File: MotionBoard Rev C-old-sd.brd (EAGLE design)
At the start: 99 x 53.3 mm, 110 parts, among them IC1 LPC1769FBD100 or LPC4078FBD10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, IC2 LD1117, IC4 LMV324, Q1 NTGS3441T1G, Q2 12MHz, Q3 25MHz, U1 ARDUINO-FIREPICK+RAMPS, U2 101-00660-68-6, X2 USB-MICRO-B

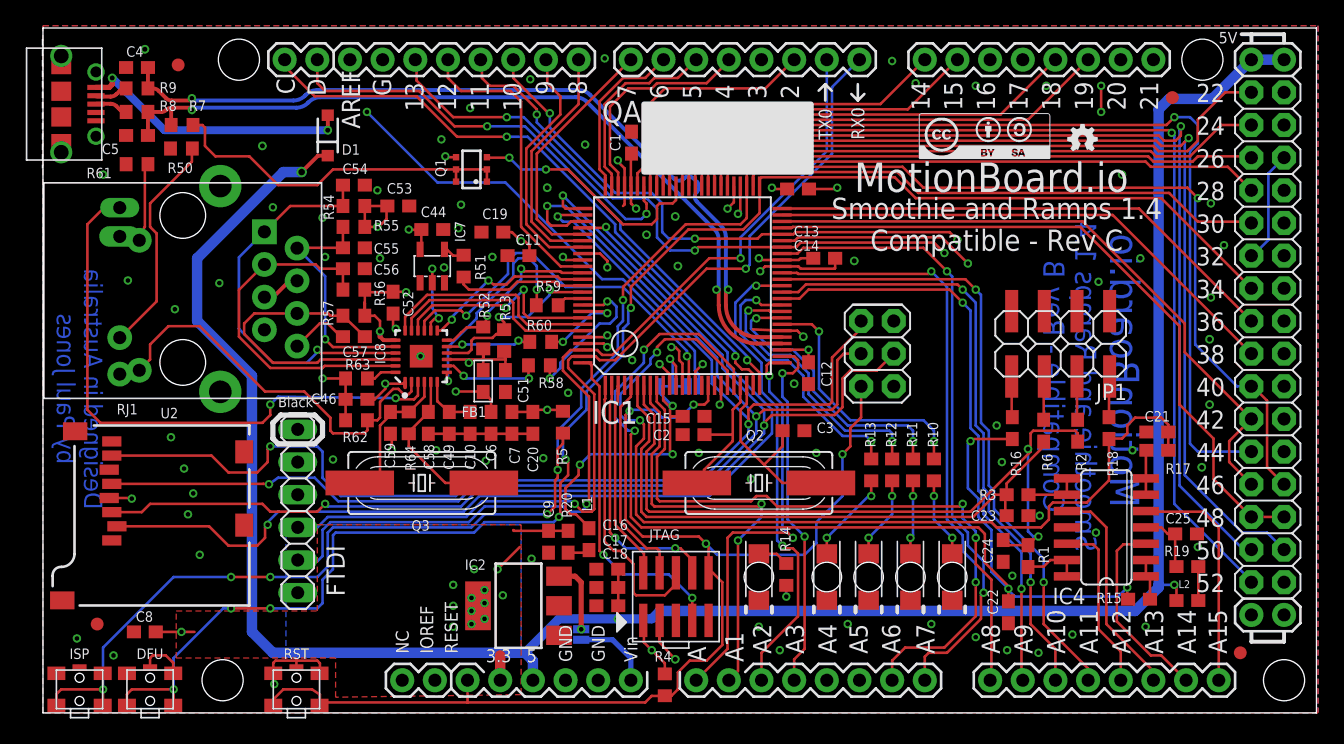
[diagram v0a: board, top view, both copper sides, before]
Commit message: Update component values
Signed-off-by: Paul Jones <paul@pauljones.id.au>
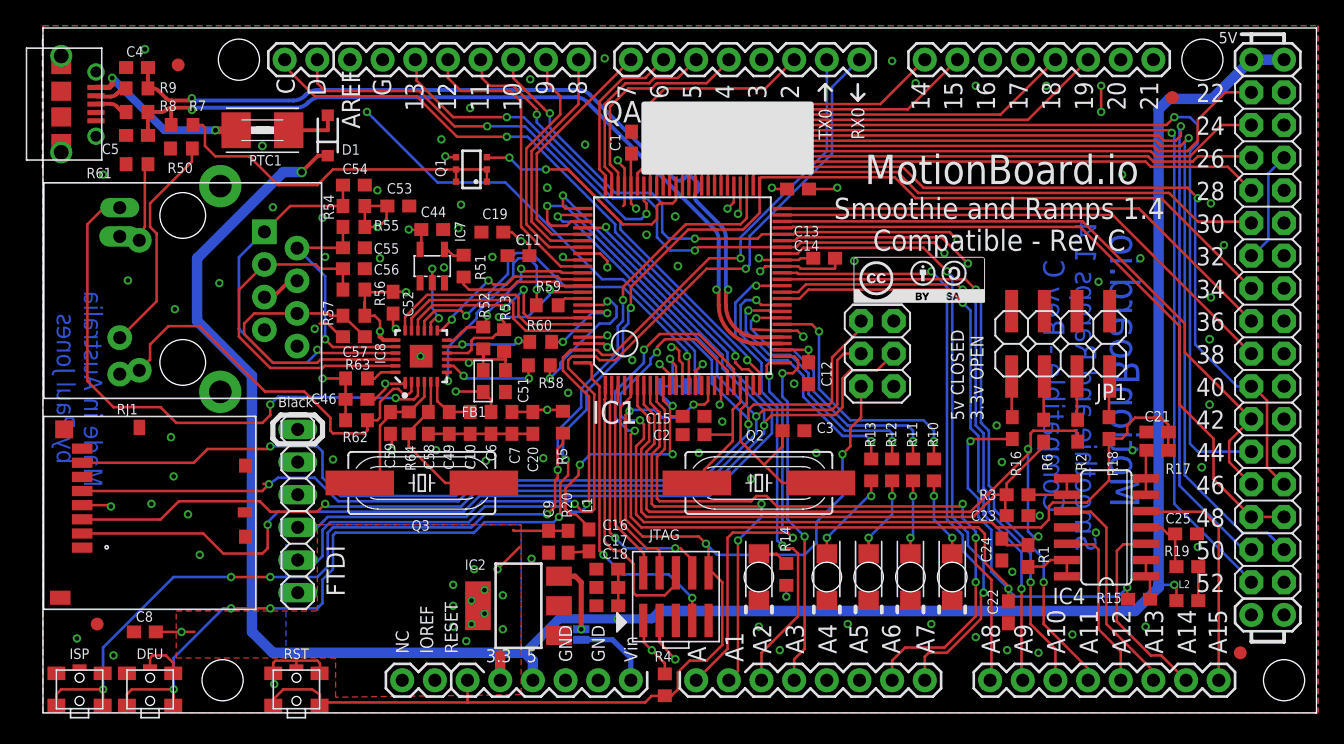
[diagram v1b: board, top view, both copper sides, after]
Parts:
- removed LOGO10, LOGO2: LOGO-OSHWSMALL, FirePick:LOGO-OSHW-SMALL
- removed LOGO3: LOGO-CC-BY-SAMEDIUM, FirePick:LOGO-CC-BY-SA-MEDIUM
- removed U2: 101-00660-68-6, SparkFun-Connectors:MICRO-SD-SOCKET-PP
- added PTC1: (no value), adafruit:1812
- added X1: ST9S008V4AR1500, ST9S008V4AR1500-598396:ST9S008V4AR1500
- R1, R15, R17, R3: value 170k -> 17k
- R16, R18, R2, R6: value 330k -> 33k
- moved LOGO6 12.3 mm to (63.0, 31.9)
- moved C24 0.14 mm to (74.6, 12.7)
- moved L1 0.10 mm to (42.5, 13.4)
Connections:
- new net N$22: RJ1.GND
- new net N$9: PTC1.2, X2.1
- net 3.3V: now also X1.4; no longer U2.4
- net GND: now also X1.6, X1.ID; no longer RJ1.GND, U2.6, U2.GND1, U2.GND3
- net SD_CS: now also X1.2; no longer U2.2
- net SD_MISO: now also X1.7; no longer U2.7
- net SD_MOSI: now also X1.3; no longer U2.3
- net SD_SCK: now also X1.5; no longer U2.5
- net VUSB: now also PTC1.1; no longer X2.1
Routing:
- net VUSB: track 21.5 -> 4.22 mm, vias 2 -> 0
- net N$9: track 0.00 -> 13.4 mm, vias 0 -> 2
- net SD_CS: track 79.1 -> 82.6 mm
- net SD_SCK: track 94.9 -> 97.8 mm
- net SD_MOSI: track 95.2 -> 97.9 mm
- net GND: track 65.4 -> 62.9 mm, vias 87 -> 89
- net LED1/REGOFF: track 46.1 -> 44.8 mm
- net SD_MISO: track 96.9 -> 97.8 mm
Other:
- board text added: "Made in Australia by Paul Jones"
- board text removed: "Designed in Australia by Paul Jones"
- board text removed: "Smoothie and Ramps 1.4 Compatible - Rev B"

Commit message: Update component values
Signed-off-by: Paul Jones <paul@pauljones.id.au>
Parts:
- R52, R7: value 1.5k -> 1k
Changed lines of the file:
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@@
 <attribute name="VALUE" x="30.6832" y="35.6362" size="1.27" layer="27" rot="R270"/>
 </element>
-<element name="R52" library="resistor" package="R0603" value="1.5k" x="34.2392" y="29.1592" smashed="yes" rot="R270">
+<element name="R52" library="resistor" package="R0603" value="1k" x="34.2392" y="29.1592" smashed="yes" rot="R270">
 <attribute name="NAME" x="33.909" y="32.6898" size="0.8128" layer="25" rot="R270"/>
 <attribute name="VALUE" x="32.2072" y="30.0482" size="1.27" layer="27" rot="R270"/>
@@
 <attribute name="VALUE" x="30.48" y="21.6662" size="1.27" layer="27" rot="R90"/>
 </element>
-<element name="R7" library="resistor" package="R0603" value="1.5k" x="10.8204" y="45.72" smashed="yes">
+<element name="R7" library="resistor" package="R0603" value="1k" x="10.8204" y="45.72" smashed="yes">
 <attribute name="NAME" x="11.3538" y="46.8122" size="0.8128" layer="25"/>
 <attribute name="VALUE" x="9.9314" y="43.688" size="1.27" layer="27"/>
